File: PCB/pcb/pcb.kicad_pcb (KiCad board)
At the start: 2 copper layers, 78 x 78 mm, 8 parts, among them J1 Reed, J2 Button, J3 LED, J4 Servo Signal, U1 NodeMCU1.0(ESP-12E), U2 ACS712xLCTR-30A

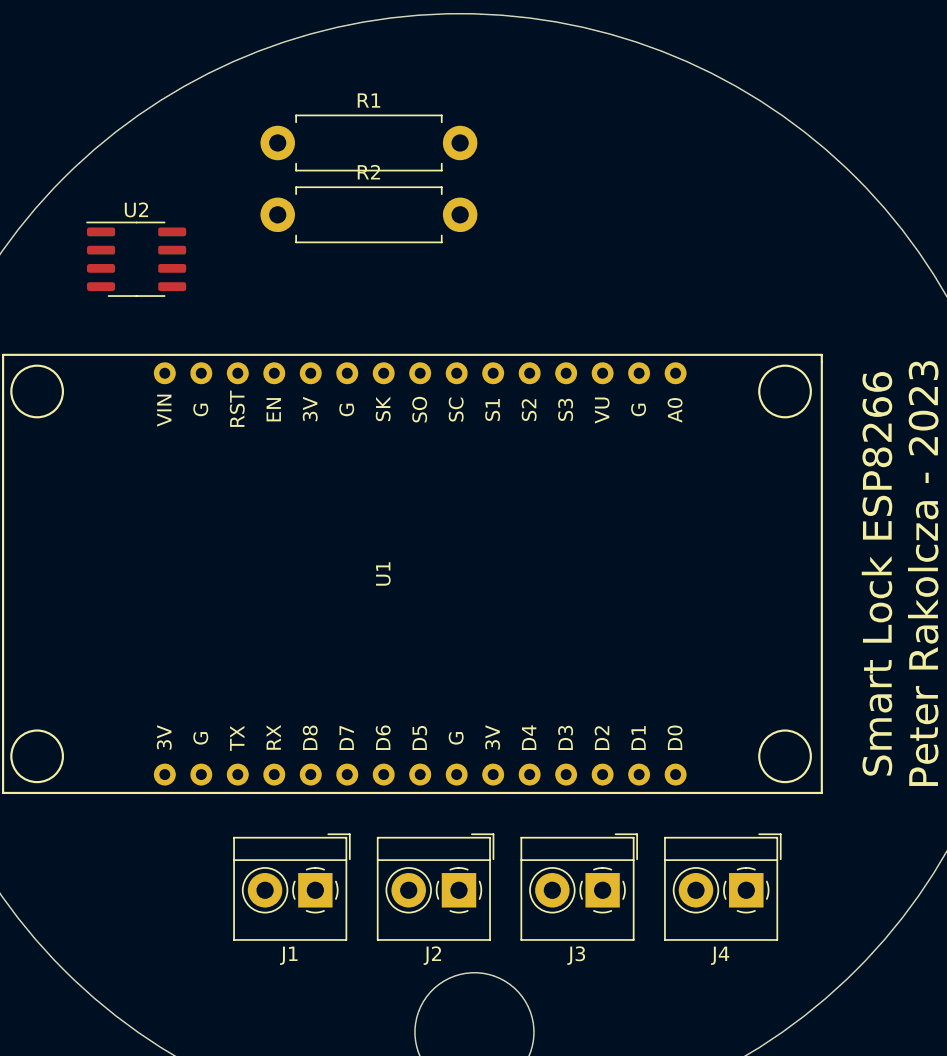
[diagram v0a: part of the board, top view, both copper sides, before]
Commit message: updated the PCB
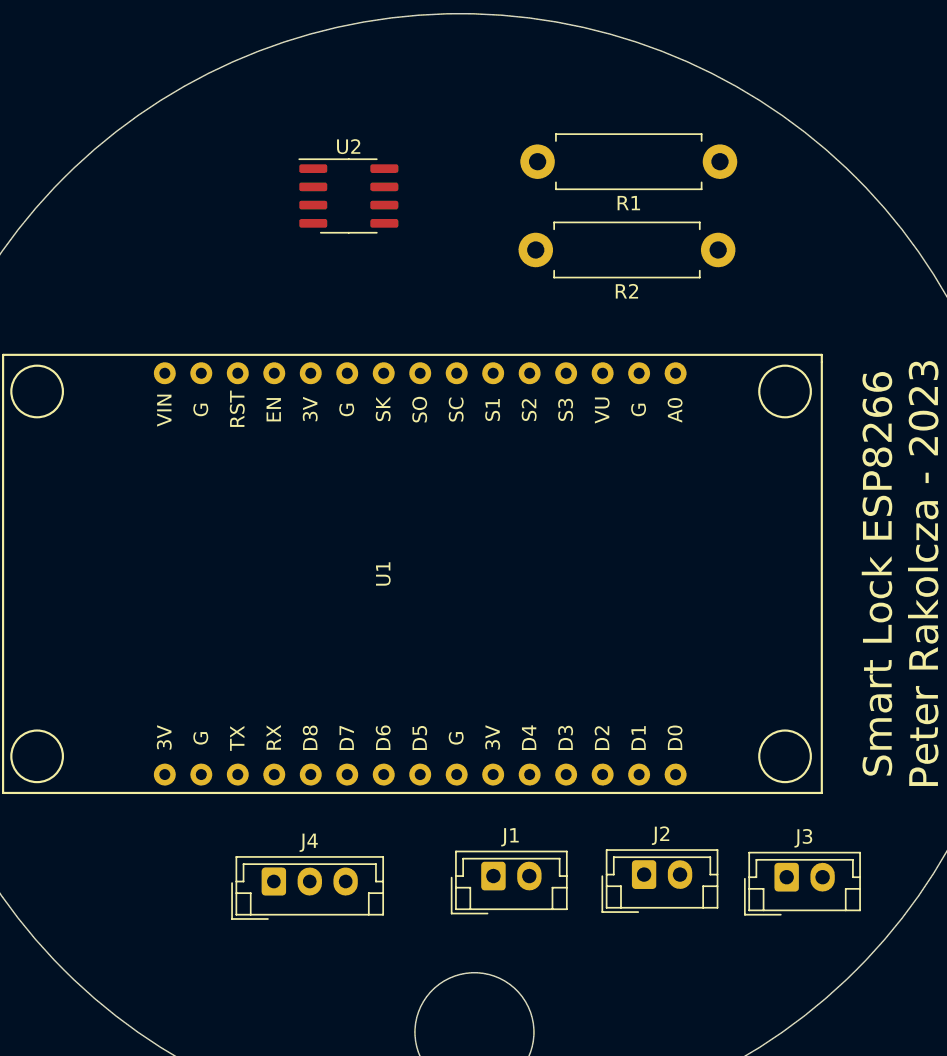
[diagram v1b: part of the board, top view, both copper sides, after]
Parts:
- J1, J2, J3: footprint TerminalBlock_4Ucon:TerminalBlock_4Ucon_1x02_P3.50mm_Horizontal -> Connector_JST:JST_EH_B2B-EH-A_1x02_P2.50mm_Vertical
- J4: value Servo Signal -> Servo; footprint TerminalBlock_4Ucon:TerminalBlock_4Ucon_1x02_P3.50mm_Horizontal -> Connector_JST:JST_EH_B3B-EH-A_1x03_P2.50mm_Vertical
- moved J4 32.9 mm to (62.0, 126.4), turned to 0 degrees
- moved R1 30.8 mm to (93.1, 76.3), turned to 180 degrees
- moved R2 30.8 mm to (93.0, 82.4), turned to 180 degrees
- moved U2 15.4 mm to (67.2, 78.7)
- moved J2 12.9 mm to (87.8, 125.9), turned to 0 degrees
- moved J3 12.8 mm to (97.7, 126.1), turned to 0 degrees
- moved J1 12.4 mm to (77.3, 126.0), turned to 0 degrees
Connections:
- J2 pad 1: Net-(J2-Pin_1) -> Net-(J1-Pin_1)
- J2 pad 2: Net-(J1-Pin_2) -> Net-(J2-Pin_2)
- J3 pad 1: Net-(J3-Pin_1) -> Net-(J1-Pin_1)
- J3 pad 2: Net-(J1-Pin_2) -> Net-(J3-Pin_2)
- J4 pad 2: unconnected-(J4-Pin_2-Pad2) -> Net-(J4-Pin_2)
- U1 pad 17: unconnected-(U1-GND-Pad17) -> Net-(J4-Pin_1)
- U1 pad 24: Net-(J1-Pin_2) -> Net-(J1-Pin_1)
- U1 pad 26: Net-(J4-Pin_1) -> Net-(J4-Pin_3)
- U1 pad 27: Net-(J1-Pin_1) -> Net-(J1-Pin_2)
- U1 pad 28: Net-(J2-Pin_1) -> Net-(J2-Pin_2)
- U1 pad 29: Net-(J3-Pin_1) -> Net-(J3-Pin_2)
- U2 pad 1: Net-(U2-IP+-Pad1) -> Net-(U1-VIN)
- U2 pad 2: Net-(U2-IP+-Pad1) -> Net-(U1-VIN)
- U2 pad 3: Net-(U2-IP--Pad3) -> Net-(J4-Pin_2)
- U2 pad 4: Net-(U2-IP--Pad3) -> Net-(J4-Pin_2)

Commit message: finished PCB design
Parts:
- added M3: MountingHole_3.2mm_M3, MountingHole:MountingHole_3.2mm_M3, F.Cu at (48.7, 125.8)
- added M3: MountingHole_3.2mm_M3, MountingHole:MountingHole_3.2mm_M3, F.Cu at (74.2, 71.6)
- J1, J2, J3: footprint Connector_JST:JST_EH_B2B-EH-A_1x02_P2.50mm_Vertical -> Connector_PinHeader_2.54mm:PinHeader_1x02_P2.54mm_Vertical
- J4: footprint Connector_JST:JST_EH_B3B-EH-A_1x03_P2.50mm_Vertical -> Connector_PinHeader_2.54mm:PinHeader_1x03_P2.54mm_Vertical
- moved J1 7.40 mm to (70.4, 128.6)
- moved J2 6.27 mm to (82.1, 128.6)
- moved J3 4.58 mm to (93.9, 128.6)
- moved J4 3.53 mm to (58.6, 127.3)
- moved U2 2.23 mm to (65.1, 79.1)
- moved R2 0.13 mm to (93.1, 82.4)
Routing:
- net Net-(J4-Pin_2): track 0.00 -> 60.7 mm, vias 0 -> 1
- net Net-(J1-Pin_1): track 0.00 -> 36.1 mm
- net Net-(U2-GND): track 0.00 -> 28.1 mm
- net Net-(J4-Pin_3): track 0.00 -> 26.8 mm
- net Net-(U1-VIN): track 0.00 -> 22.3 mm
- net Net-(J1-Pin_2): track 0.00 -> 21.1 mm
- net Net-(U1-A0(ADC0)): track 0.00 -> 16.0 mm
- net Net-(J3-Pin_2): track 0.00 -> 14.8 mm
- net Net-(U2-VIOUT): track 0.00 -> 13.8 mm
- net Net-(J2-Pin_2): track 0.00 -> 13.3 mm
- net Net-(J4-Pin_1): track 0.00 -> 9.03 mm
- added copper zone on B.Cu, net Net-(U2-GND)
- added copper zone on F.Cu, net Net-(U2-GND)
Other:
- outline, holes or cut-outs redrawn
- board text added: "3.3V"
- board text added: "Button"
- board text added: "G"
- board text added: "LED"
- board text added: "Reed"
- board text added: "Servo"
- board text added: "Signal"
- board text added: "VIN"
